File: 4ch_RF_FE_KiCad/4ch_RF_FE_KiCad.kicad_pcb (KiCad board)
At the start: 4 copper layers, 249.9 x 94.7 mm, 286 parts, among them J1 PJ1-021-SMT-TR, J10 5-1814832-1, J11 5-1814832-1, J12 5-1814832-1, J13 5-1814832-1, J14 5-1814832-1, J15 5-1814832-1, J16 5-1814832-1, J17 5-1814832-1, J18 5-1814832-1, J19 5-1814832-1, J2 PPTC062LJBN-RC, J20 5-1814832-1, J21 5-1814832-1, J22 5-1814832-1, J3 5-1814832-1, J4 5-1814832-1, J5 5-1814832-1, J6 5-1814832-1, J7 5-1814832-1, J8 5-1814832-1, J9 5-1814832-1, T1 MABA-011082, T2 MABA-011082, T3 MABA-011082, T4 MABA-011082, T5 MABA-011082, T6 MABA-011082, T7 MABA-011082, T8 MABA-011082, U1 SOT-223_3MC, U10 PW14, U11 RK_3, U12 PE43711, U13 HMC544AETR, U14 RK_3, U15 PE43711, U16 HMC544AETR, U17 HMC544AETR, U18 PCAL6416APW, U19 RK_3, U2 SOT-223_3MC, U20 PE43711, U21 HMC544AETR, U22 RK_3, U23 PE43711, U24 HMC544AETR, U25 HMC544AETR, U26 PCAL6416APW, U27 RK_3, U28 PE43711, U29 HMC544AETR, U3 SOT-223_3MC, U30 RK_3, U31 PE43711, U32 HMC544AETR, U33 HMC544AETR, U34 PCAL6416APW, U35 RK_3, U36 PE43711, U37 HMC544AETR, U38 RK_3, U39 PE43711, U4 SOT-223_3MC, U40 HMC544AETR, U41 HMC544AETR, U42 PCAL6416APW, U5 INA219AIDCNR, U6 DDC0006A_N, U7 PCA9548APW, U8 M24C02-FDW, U9 PW14

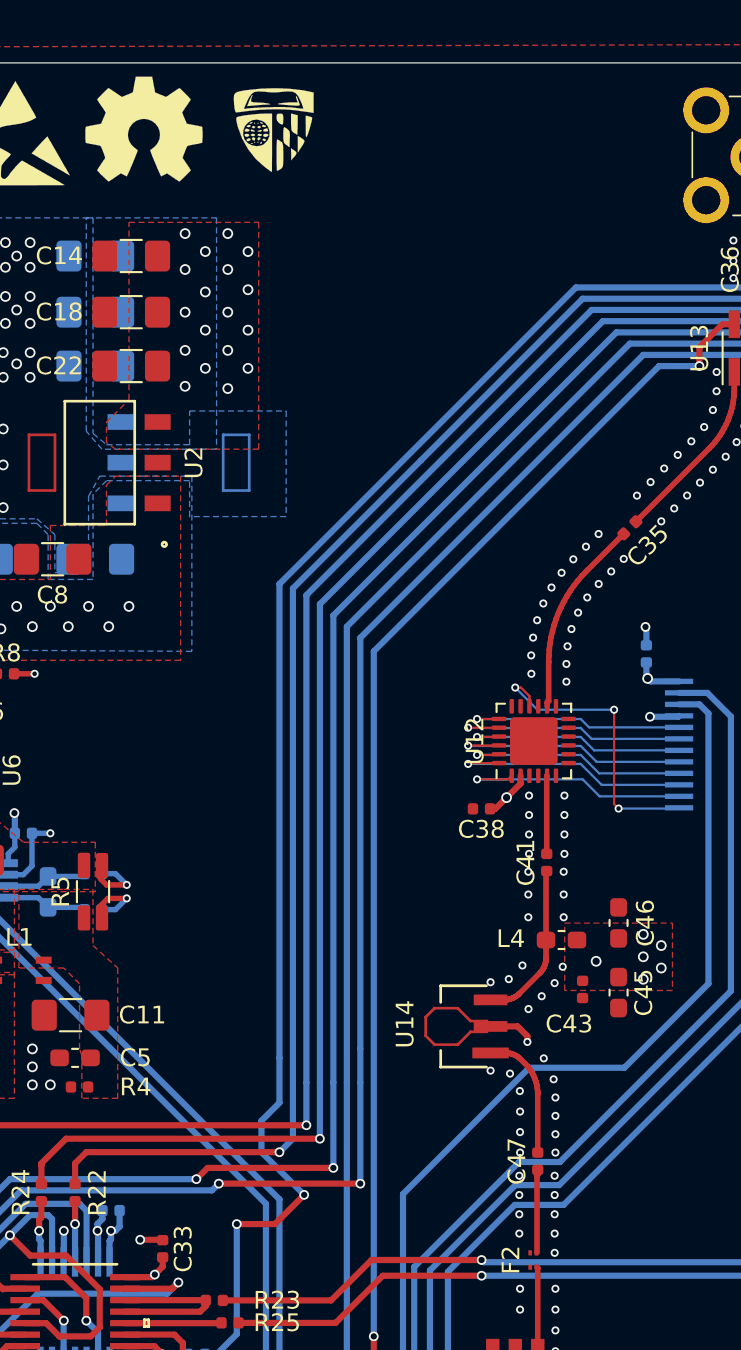
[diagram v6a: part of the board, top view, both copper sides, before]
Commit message: (+) QR code -> shipped to OSH Park
Signed-off-by: Gentile, John <johncgentile17@gmail.com>
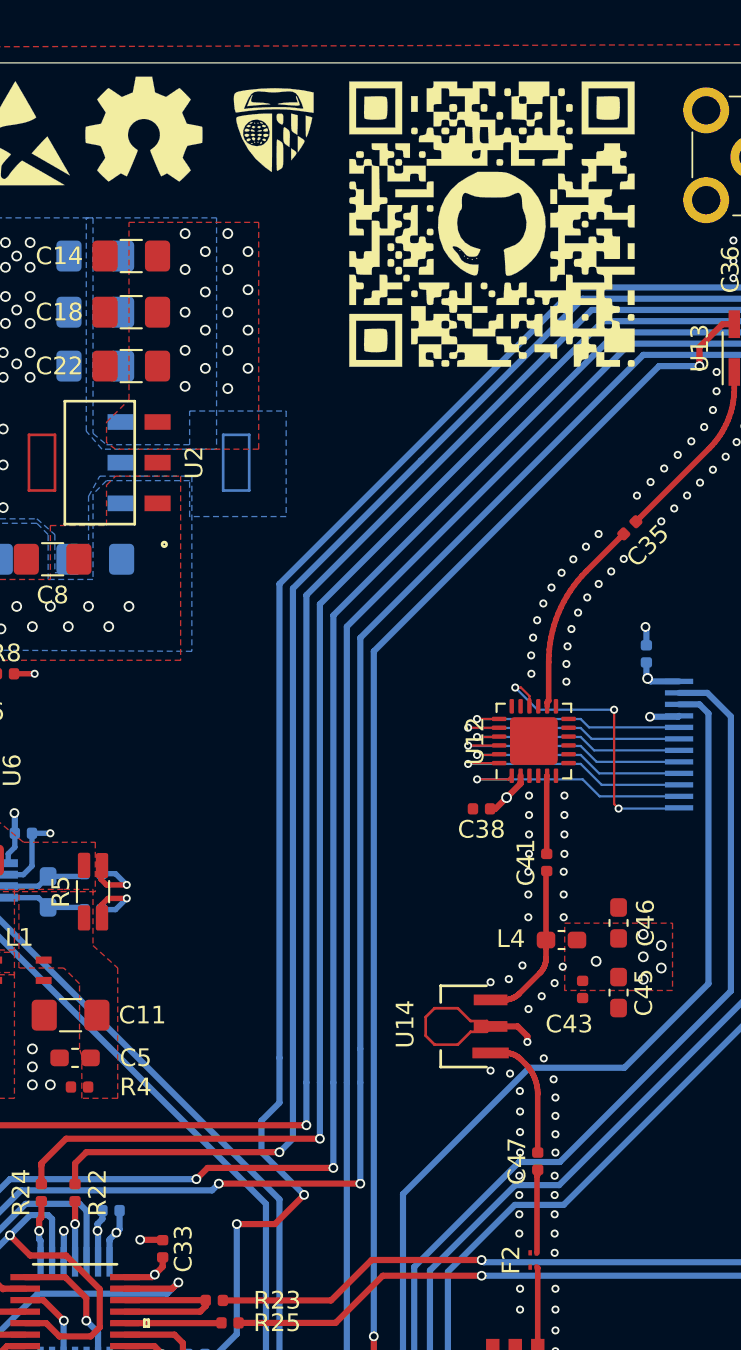
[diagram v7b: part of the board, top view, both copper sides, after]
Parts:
- added G***: LOGO, jcg_custom:github_QR_code, F.Cu at (86.9, 106.4)
